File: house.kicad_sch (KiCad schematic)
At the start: 10 parts, among them U3 LMR36510ADDA

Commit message: For Darrel
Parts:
- renumbered C37 to C10, C31 to C4, C32 to C5, C33 to C6, C34 to C7, C35 to C8, C36 to C9, L2 to L1, R16 to R6, U3 to U4

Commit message: Round 1 review comments
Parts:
- renumbered C4 to C11, C5 to C12, C6 to C13, C7 to C14, C8 to C15, C9 to C16, C10 to C17, L1 to L2, R6 to R7, U4 to U5
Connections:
- net SET is gone; now on net VOUT: R7.2
- net FB: now reaches R7.1, U5.5 (FB)
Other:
- moved on the sheet: C15, C16, C17, R7

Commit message: Round 2 Review, power tree cleanup
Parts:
- renumbered C11 to C194, C12 to C195, C13 to C196, C14 to C197, C15 to C198, C16 to C199, C17 to C200, L2 to L7, R7 to R226, U5 to U33
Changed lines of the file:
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@@
 		(dnp no)
 		(fields_autoplaced yes)
-		(property "Reference" "C13"
+		(property "Reference" "C196"
 			(at 119.38 92.7162 0)
 			(show_name no)
@@
 			(project "huskypointofload"
 				(path "/eb9c972b-d134-41da-be97-ece3f463f7e0/aad3f0e3-dcbe-4112-94dc-37caa60c9eb1/a6897837-f484-4895-9d17-f1bafbc2e4e6"
-					(reference "C13")
+					(reference "C196")
 					(unit 1)
 				)
@@
 		(in_pos_files yes)
 		(dnp no)
-		(property "Reference" "C11"
+		(property "Reference" "C194"
 			(at 100.33 82.5562 0)
 			(show_name no)
@@
 			(project "huskypointofload"
 				(path "/eb9c972b-d134-41da-be97-ece3f463f7e0/aad3f0e3-dcbe-4112-94dc-37caa60c9eb1/a6897837-f484-4895-9d17-f1bafbc2e4e6"
-					(reference "C11")
+					(reference "C194")
 					(unit 1)
 				)
@@
 		(dnp no)
 		(fields_autoplaced yes)
-		(property "Reference" "C16"
+		(property "Reference" "C199"
 			(at 179.07 85.0962 0)
 			(show_name no)
@@
 			(project "huskypointofload"
 				(path "/eb9c972b-d134-41da-be97-ece3f463f7e0/aad3f0e3-dcbe-4112-94dc-37caa60c9eb1/a6897837-f484-4895-9d17-f1bafbc2e4e6"
-					(reference "C16")
+					(reference "C199")
 					(unit 1)
 				)
@@
 		(dnp no)
 		(fields_autoplaced yes)
-		(property "Reference" "C17"
+		(property "Reference" "C200"
 			(at 187.96 85.0962 0)
 			(show_name no)
@@
 			(project "huskypointofload"
 				(path "/eb9c972b-d134-41da-be97-ece3f463f7e0/aad3f0e3-dcbe-4112-94dc-37caa60c9eb1/a6897837-f484-4895-9d17-f1bafbc2e4e6"
-					(reference "C17")
+					(reference "C200")
 					(unit 1)
 				)
@@
 		(dnp no)
 		(fields_autoplaced yes)
-		(property "Reference" "U5"
+		(property "Reference" "U33"
 			(at 130.81 71.12 0)
 			(show_name no)
@@
 			(project "huskypointofload"
 				(path "/eb9c972b-d134-41da-be97-ece3f463f7e0/aad3f0e3-dcbe-4112-94dc-37caa60c9eb1/a6897837-f484-4895-9d17-f1bafbc2e4e6"
-					(reference "U5")
+					(reference "U33")
 					(unit 1)
 				)
@@
 		(in_pos_files yes)
 		(dnp no)
-		(property "Reference" "R7"
+		(property "Reference" "R226"
 			(at 156.21 91.44 90)
 			(show_name no)
@@
 			(project "huskypointofload"
 				(path "/eb9c972b-d134-41da-be97-ece3f463f7e0/aad3f0e3-dcbe-4112-94dc-37caa60c9eb1/a6897837-f484-4895-9d17-f1bafbc2e4e6"
-					(reference "R7")
+					(reference "R226")
 					(unit 1)
 				)
@@
 		(dnp no)
 		(fields_autoplaced yes)
-		(property "Reference" "C14"
+		(property "Reference" "C197"
 			(at 146.0563 72.39 90)
 			(show_name no)
@@
 			(project "huskypointofload"
 				(path "/eb9c972b-d134-41da-be97-ece3f463f7e0/aad3f0e3-dcbe-4112-94dc-37caa60c9eb1/a6897837-f484-4895-9d17-f1bafbc2e4e6"
-					(reference "C14")
+					(reference "C197")
 					(unit 1)
 				)
@@
 		(dnp no)
 		(fields_autoplaced yes)
-		(property "Reference" "C15"
+		(property "Reference" "C198"
 			(at 170.18 85.0962 0)
 			(show_name no)
@@
 			(project "huskypointofload"
 				(path "/eb9c972b-d134-41da-be97-ece3f463f7e0/aad3f0e3-dcbe-4112-94dc-37caa60c9eb1/a6897837-f484-4895-9d17-f1bafbc2e4e6"
-					(reference "C15")
+					(reference "C198")
 					(unit 1)
 				)
@@
 		(dnp no)
 		(fields_autoplaced yes)
-		(property "Reference" "#PWR020"
+		(property "Reference" "#PWR0247"
 			(at 130.81 107.95 0)
 			(hide yes)
@@
 			(project "huskypointofload"
 				(path "/eb9c972b-d134-41da-be97-ece3f463f7e0/aad3f0e3-dcbe-4112-94dc-37caa60c9eb1/a6897837-f484-4895-9d17-f1bafbc2e4e6"
-					(reference "#PWR020")
+					(reference "#PWR0247")
 					(unit 1)
 				)
@@
 		(dnp no)
 		(fields_autoplaced yes)
-		(property "Reference" "L2"
+		(property "Reference" "L7"
 			(at 156.21 76.2 90)
 			(show_name no)
@@
 			(project "huskypointofload"
 				(path "/eb9c972b-d134-41da-be97-ece3f463f7e0/aad3f0e3-dcbe-4112-94dc-37caa60c9eb1/a6897837-f484-4895-9d17-f1bafbc2e4e6"
-					(reference "L2")
+					(reference "L7")
 					(unit 1)
 				)
@@
 		(dnp no)
 		(fields_autoplaced yes)
-		(property "Reference" "C12"
+		(property "Reference" "C195"
 			(at 110.49 82.5562 0)
 			(show_name no)
@@
 			(project "huskypointofload"
 				(path "/eb9c972b-d134-41da-be97-ece3f463f7e0/aad3f0e3-dcbe-4112-94dc-37caa60c9eb1/a6897837-f484-4895-9d17-f1bafbc2e4e6"
-					(reference "C12")
-					(unit 1)
-				)
+					(reference "C195")
+					(unit 1)
+				)

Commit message: Darrel Suggestions
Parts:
- renumbered C194 to C195, C195 to C196, C196 to C197, C197 to C198, C198 to C199, C199 to C200, C200 to C201, L7 to L5
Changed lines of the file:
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@@
 		(dnp no)
 		(fields_autoplaced yes)
-		(property "Reference" "C196"
+		(property "Reference" "C197"
 			(at 119.38 92.7162 0)
 			(show_name no)
@@
 			(project "huskypointofload"
 				(path "/eb9c972b-d134-41da-be97-ece3f463f7e0/aad3f0e3-dcbe-4112-94dc-37caa60c9eb1/a6897837-f484-4895-9d17-f1bafbc2e4e6"
-					(reference "C196")
+					(reference "C197")
 					(unit 1)
 				)
@@
 		(in_pos_files yes)
 		(dnp no)
-		(property "Reference" "C194"
+		(property "Reference" "C195"
 			(at 100.33 82.5562 0)
 			(show_name no)
@@
 			(project "huskypointofload"
 				(path "/eb9c972b-d134-41da-be97-ece3f463f7e0/aad3f0e3-dcbe-4112-94dc-37caa60c9eb1/a6897837-f484-4895-9d17-f1bafbc2e4e6"
-					(reference "C194")
+					(reference "C195")
 					(unit 1)
 				)
@@
 		(dnp no)
 		(fields_autoplaced yes)
-		(property "Reference" "C199"
+		(property "Reference" "C200"
 			(at 179.07 85.0962 0)
 			(show_name no)
@@
 			(project "huskypointofload"
 				(path "/eb9c972b-d134-41da-be97-ece3f463f7e0/aad3f0e3-dcbe-4112-94dc-37caa60c9eb1/a6897837-f484-4895-9d17-f1bafbc2e4e6"
-					(reference "C199")
+					(reference "C200")
 					(unit 1)
 				)
@@
 		(dnp no)
 		(fields_autoplaced yes)
-		(property "Reference" "C200"
+		(property "Reference" "C201"
 			(at 187.96 85.0962 0)
 			(show_name no)
@@
 			(project "huskypointofload"
 				(path "/eb9c972b-d134-41da-be97-ece3f463f7e0/aad3f0e3-dcbe-4112-94dc-37caa60c9eb1/a6897837-f484-4895-9d17-f1bafbc2e4e6"
-					(reference "C200")
+					(reference "C201")
 					(unit 1)
 				)
@@
 		(dnp no)
 		(fields_autoplaced yes)
-		(property "Reference" "C197"
+		(property "Reference" "C198"
 			(at 146.0563 72.39 90)
 			(show_name no)
@@
 			(project "huskypointofload"
 				(path "/eb9c972b-d134-41da-be97-ece3f463f7e0/aad3f0e3-dcbe-4112-94dc-37caa60c9eb1/a6897837-f484-4895-9d17-f1bafbc2e4e6"
-					(reference "C197")
+					(reference "C198")
 					(unit 1)
 				)
@@
 		(dnp no)
 		(fields_autoplaced yes)
-		(property "Reference" "C198"
+		(property "Reference" "C199"
 			(at 170.18 85.0962 0)
 			(show_name no)
@@
 			(project "huskypointofload"
 				(path "/eb9c972b-d134-41da-be97-ece3f463f7e0/aad3f0e3-dcbe-4112-94dc-37caa60c9eb1/a6897837-f484-4895-9d17-f1bafbc2e4e6"
-					(reference "C198")
+					(reference "C199")
 					(unit 1)
 				)
@@
 		(dnp no)
 		(fields_autoplaced yes)
-		(property "Reference" "#PWR0247"
+		(property "Reference" "#PWR0250"
 			(at 130.81 107.95 0)
 			(hide yes)
@@
 			(project "huskypointofload"
 				(path "/eb9c972b-d134-41da-be97-ece3f463f7e0/aad3f0e3-dcbe-4112-94dc-37caa60c9eb1/a6897837-f484-4895-9d17-f1bafbc2e4e6"
-					(reference "#PWR0247")
+					(reference "#PWR0250")
 					(unit 1)
 				)
@@
 		(dnp no)
 		(fields_autoplaced yes)
-		(property "Reference" "L7"
+		(property "Reference" "L5"
 			(at 156.21 76.2 90)
 			(show_name no)
@@
 			(project "huskypointofload"
 				(path "/eb9c972b-d134-41da-be97-ece3f463f7e0/aad3f0e3-dcbe-4112-94dc-37caa60c9eb1/a6897837-f484-4895-9d17-f1bafbc2e4e6"
-					(reference "L7")
+					(reference "L5")
 					(unit 1)
 				)
@@
 		(dnp no)
 		(fields_autoplaced yes)
-		(property "Reference" "C195"
+		(property "Reference" "C196"
 			(at 110.49 82.5562 0)
 			(show_name no)
@@
 			(project "huskypointofload"
 				(path "/eb9c972b-d134-41da-be97-ece3f463f7e0/aad3f0e3-dcbe-4112-94dc-37caa60c9eb1/a6897837-f484-4895-9d17-f1bafbc2e4e6"
-					(reference "C195")
-					(unit 1)
-				)
+					(reference "C196")
+					(unit 1)
+				)

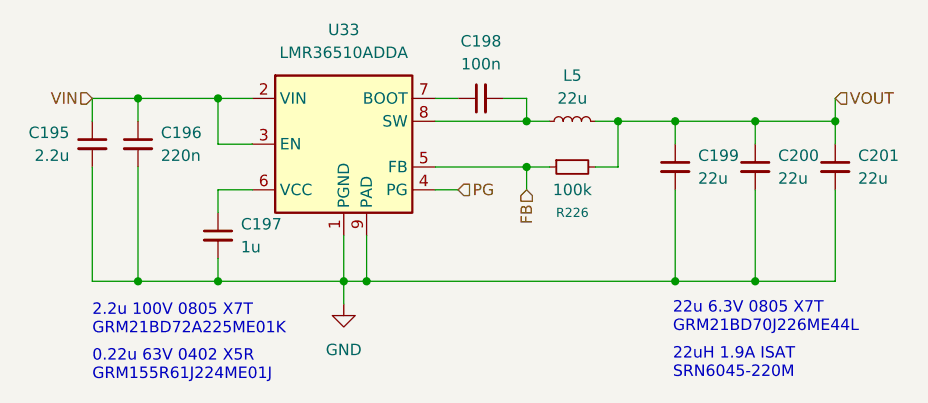
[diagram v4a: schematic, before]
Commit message: add NC and fix ERC
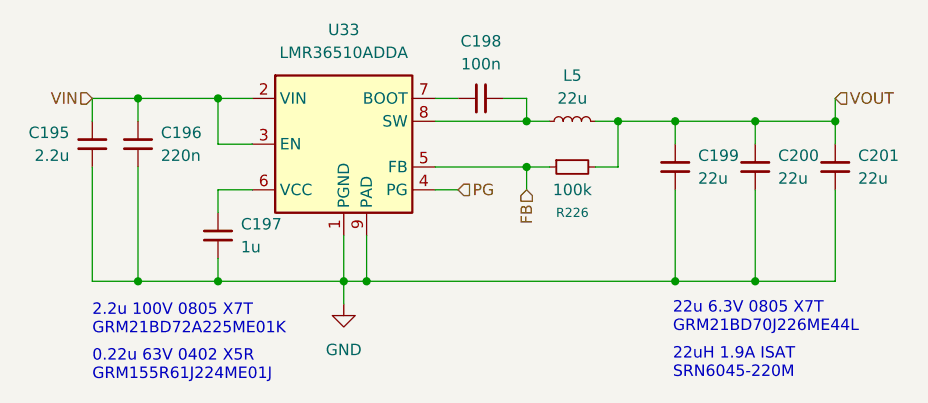
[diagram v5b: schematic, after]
